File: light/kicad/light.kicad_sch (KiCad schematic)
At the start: 106 parts, among them U1 FT4232H, U11 TLV7103318DDSE, U14 74LVC1G07, U2 SN74AVC4T774RSVR, U3 SN74AVC4T774RSVR, U4 SN74AVC4T774RSVR, U5 74LVC1G07, U6 SN74AHC595QWBQBRQ1, U7 TLV75533PDBV, U8 TLV75533PDBV, U9 93LC56BT-I/OT, Y1 12MHz_7M-12.000MAAJ

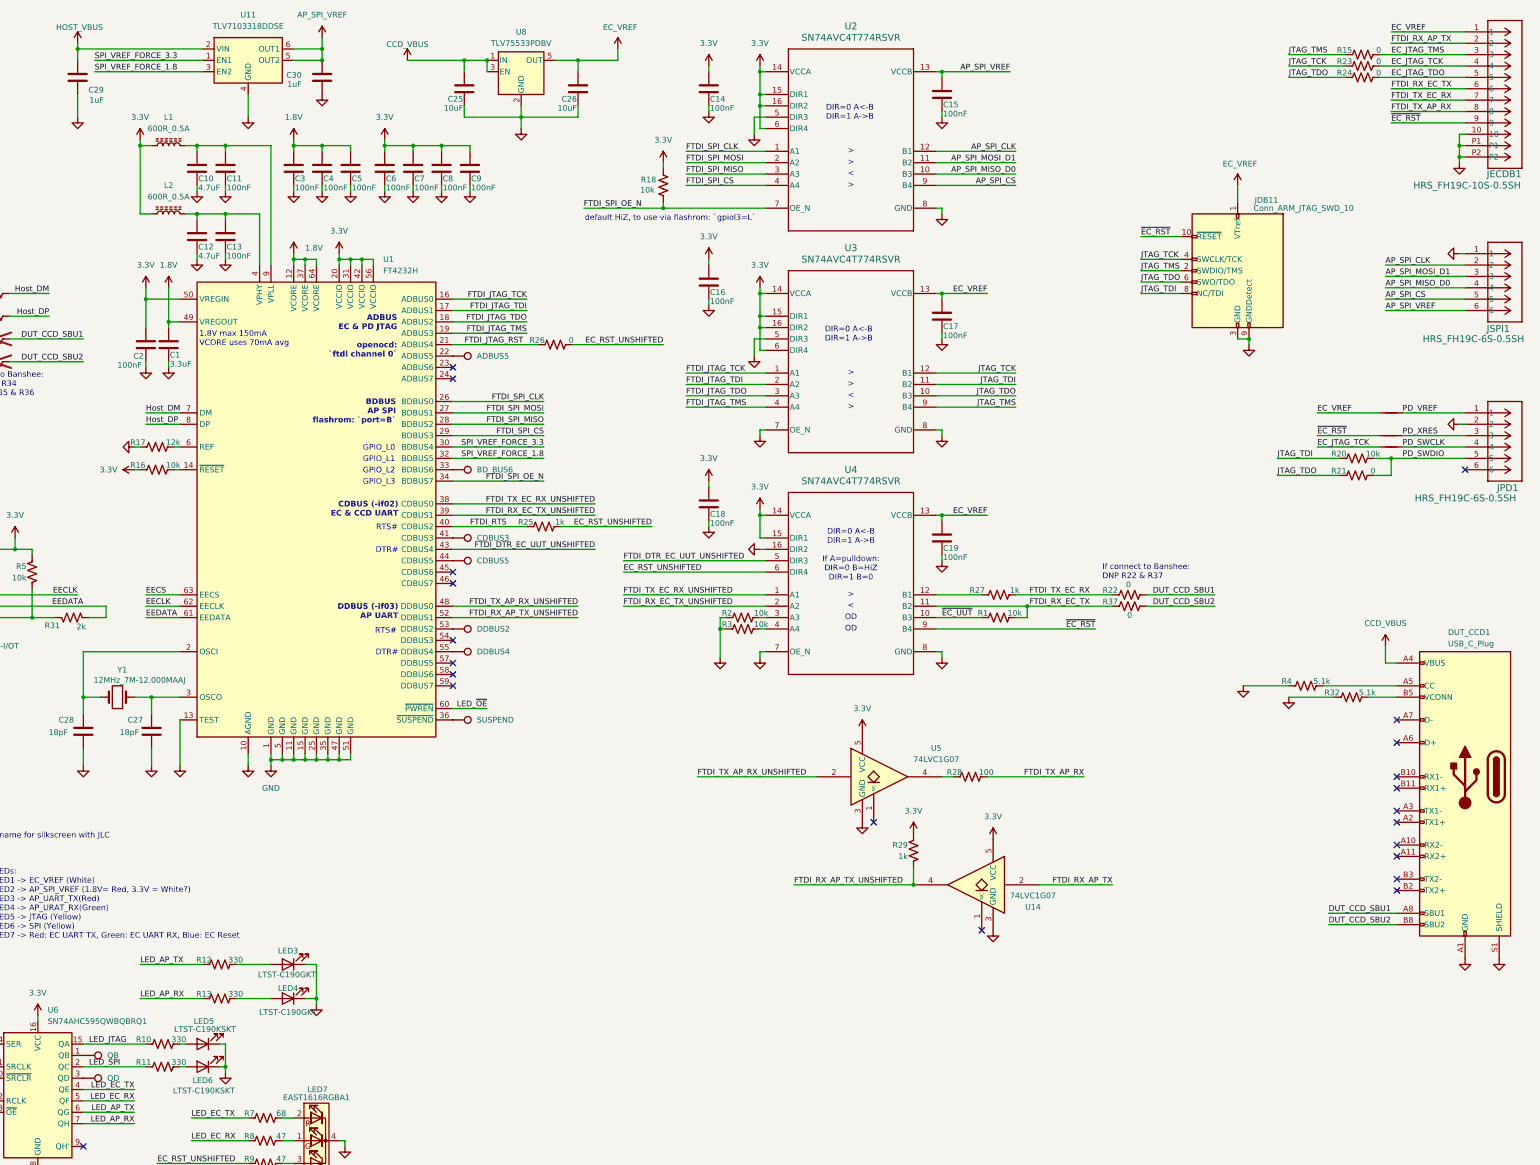
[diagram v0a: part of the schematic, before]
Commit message: kicad: renaming netname and fixing pin order of the connectors
11/05

1. Rename JTAG netname
2. Change pin order of JPD1, JSPI1, JECDB1
3. Remove TPs
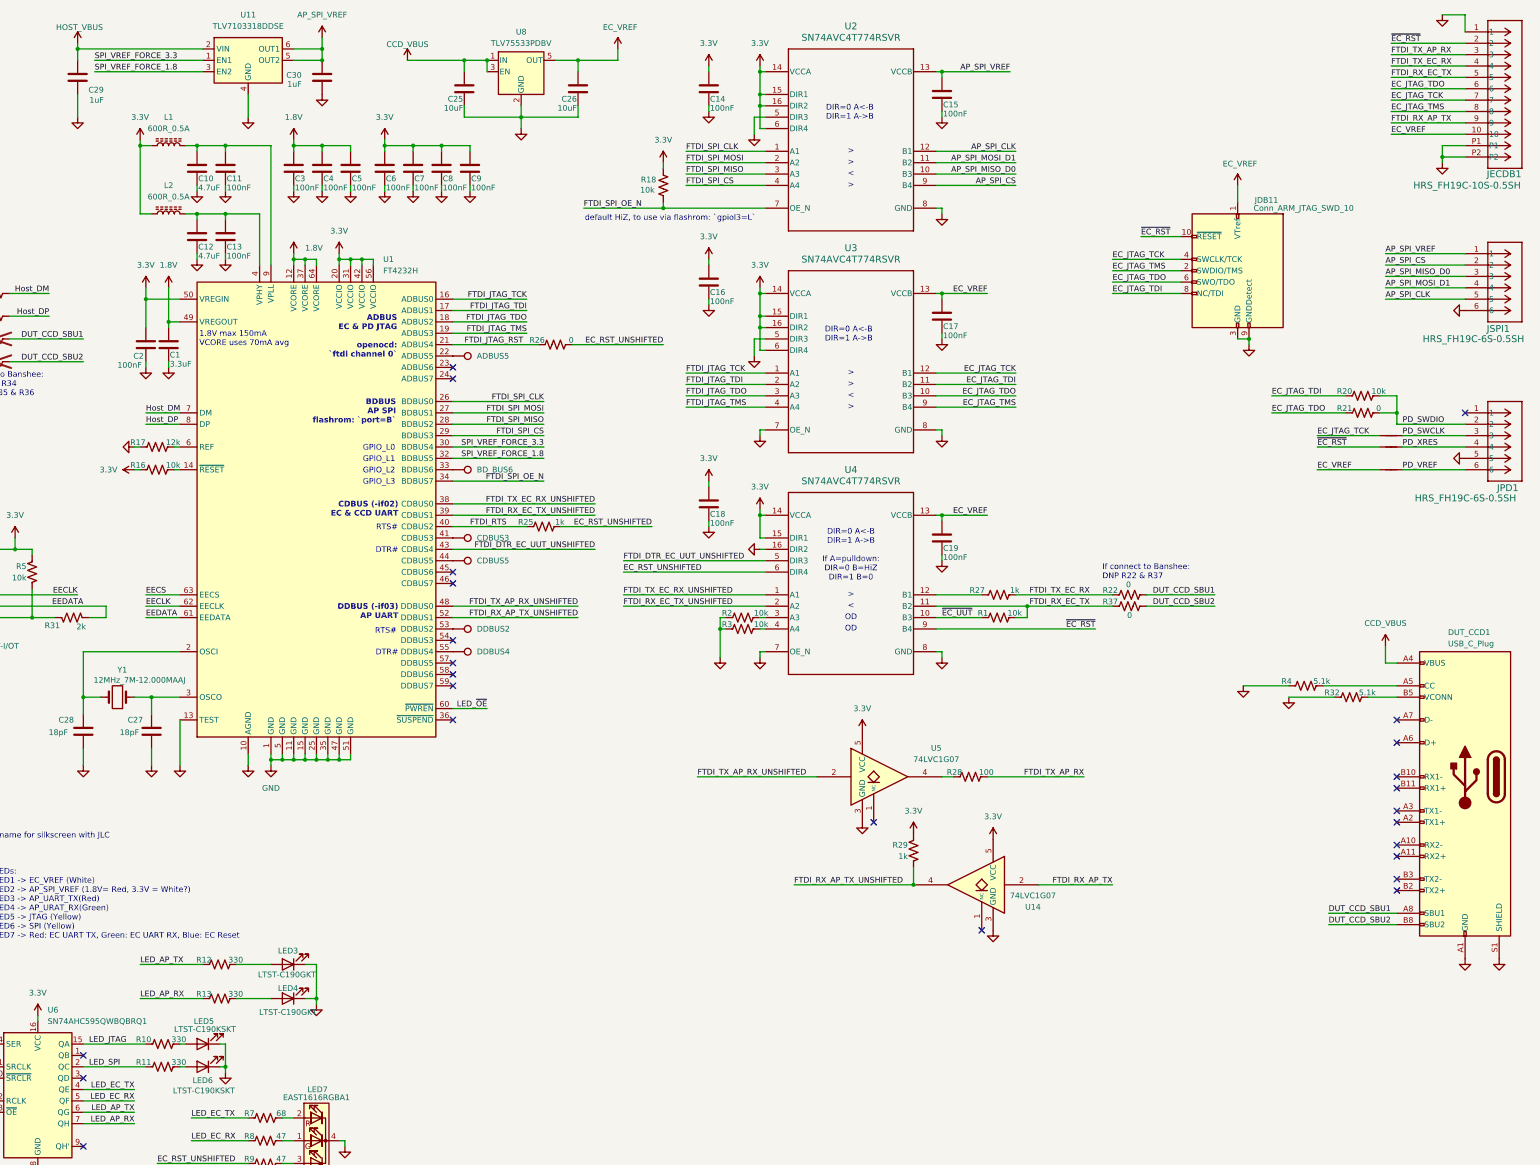
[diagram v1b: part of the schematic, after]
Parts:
- removed QB, QD, SUSPEND: TestPoint, TestPoint:TestPoint_Pad_D1.5mm, symbol Connector:TestPoint
- removed R15, R23, R24: 0, Resistor_SMD:R_0603_1608Metric, symbol Device:R_US
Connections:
- net JTAG_TCK is gone; now on net EC_JTAG_TCK: JDB11.4 (SWCLK/TCK), U3.12 (B1)
- net JTAG_TDO is gone; now on net EC_JTAG_TDO: JDB11.6 (SWO/TDO), R21.2, U3.10 (B3)
- net JTAG_TMS is gone; now on net EC_JTAG_TMS: JDB11.2 (SWDIO/TMS), U3.9 (B4)
- net AP_SPI_CLK: now also JSPI1.5; no longer JSPI1.2
- net AP_SPI_CS: now also JSPI1.2; no longer JSPI1.5
- net AP_SPI_MISO_D0: now also JSPI1.3; no longer JSPI1.4
- net AP_SPI_MOSI_D1: now also JSPI1.4; no longer JSPI1.3
- net AP_SPI_VREF: now also JSPI1.1; no longer JSPI1.6
- net EC_JTAG_TCK: now also JECDB1.7; no longer JECDB1.4
- net EC_JTAG_TDO: now also JECDB1.6; no longer JECDB1.5
- net EC_JTAG_TMS: now also JECDB1.8; no longer JECDB1.3
- net EC_VREF: now also JECDB1.10; no longer JECDB1.1
- net FTDI_RX_AP_TX: now also JECDB1.9; no longer JECDB1.2
- net FTDI_RX_EC_TX: now also JECDB1.5; no longer JECDB1.6
- net FTDI_TX_AP_RX: now also JECDB1.3; no longer JECDB1.8
- net FTDI_TX_EC_RX: now also JECDB1.4; no longer JECDB1.7
- net GND: now also JECDB1.1, JPD1.5, JSPI1.6; no longer JECDB1.10, JPD1.2, JSPI1.1
- net PD_SWCLK: now also JPD1.3; no longer JPD1.4
- net PD_SWDIO: now also JPD1.2; no longer JPD1.5
- net PD_VREF: now also JPD1.6; no longer JPD1.1
- net PD_XRES: now also JPD1.4; no longer JPD1.3
- net ~{EC_RST}: now also JECDB1.2; no longer JECDB1.9
- net JTAG_TDI renamed EC_JTAG_TDI
- no-connect marks 33 -> 36
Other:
- moved on the sheet: R20, R21

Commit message: kicad: add notes and update PCB file
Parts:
- C1, C10, C11, C12, C13, C14, C15, C16, C17, C18, C19, C2, C22, C23, C24, C25, C26, C27, C28, C29, C3, C30, C4, C5, C6, C7, C8, C9: footprint Capacitor_SMD:C_0603_1608Metric -> Capacitor_SMD:C_0201_0603Metric
- R1, R2, R20, R25, R26, R27, R28, R3: footprint Resistor_SMD:R_0603_1608Metric -> Resistor_SMD:R_0402_1005Metric
- R16, R17, R18, R21, R29, R31, R32, R4, R5, R6: footprint Resistor_SMD:R_0603_1608Metric -> Resistor_SMD:R_0201_0603Metric
- R35, R36: footprint (none) -> Resistor_SMD:R_0603_1608Metric; now fitted
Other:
- note added: "If connect to Banshee: R22 & R37 DNP R33 & R34 DNP R35 & R36 Populated else if:(default) R22 & R37 Populated R33 & R34 Populated R35 & R36 DNP"
- note removed: "If connect to Banshee: DNP R22 & R37"
- note removed: "If connect to Banshee: DNP R33 & R34 Populate R35 & R36"
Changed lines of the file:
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@@
 		)
 	)
-	(text "If connect to Banshee:\nDNP R22 & R37"
+	(text "If connect to Banshee:\nR22 & R37 DNP \nR33 & R34 DNP \nR35 & R36 Populated\n\nelse if:(default)\nR22 & R37 Populated \nR33 & R34 Populated \nR35 & R36 DNP\n"
 		(exclude_from_sim no)
-		(at 312.674 138.43 0)
+		(at 311.404 130.302 0)
 		(effects
 			(font
@@
 		)
 	)
-	(text "If connect to Banshee:\nDNP R33 & R34\nPopulate R35 & R36"
+	(text "If connect to Banshee:\nR22 & R37 DNP \nR33 & R34 DNP \nR35 & R36 Populated\n\nelse if:(default)\nR22 & R37 Populated \nR33 & R34 Populated \nR35 & R36 DNP\n"
 		(exclude_from_sim no)
-		(at 56.642 96.52 0)
+		(at 54.864 103.632 0)
 		(effects
 			(font
@@
 			)
 		)
-		(property "Footprint" "Resistor_SMD:R_0603_1608Metric"
+		(property "Footprint" "Resistor_SMD:R_0402_1005Metric"
 			(at 232.156 149.606 90)
 			(effects
@@
 			)
 		)
-		(property "Footprint" "Capacitor_SMD:C_0603_1608Metric"
+		(property "Footprint" "Capacitor_SMD:C_0201_0603Metric"
 			(at 139.3952 52.07 0)
 			(effects
@@
 			)
 		)
-		(property "Footprint" "Capacitor_SMD:C_0603_1608Metric"
+		(property "Footprint" "Capacitor_SMD:C_0201_0603Metric"
 			(at 277.8252 85.09 0)
 			(effects
@@
 			)
 		)
-		(property "Footprint" "Resistor_SMD:R_0603_1608Metric"
+		(property "Footprint" "Resistor_SMD:R_0201_0603Metric"
 			(at 213.614 51.816 90)
 			(effects
@@
 			)
 		)
-		(property "Footprint" "Resistor_SMD:R_0603_1608Metric"
+		(property "Footprint" "Resistor_SMD:R_0201_0603Metric"
 			(at 82.296 147.574 90)
 			(effects
@@
 			)
 		)
-		(property "Footprint" "Capacitor_SMD:C_0603_1608Metric"
+		(property "Footprint" "Capacitor_SMD:C_0201_0603Metric"
 			(at 169.2148 34.29 0)
 			(effects
@@
 			)
 		)
-		(property "Footprint" "Resistor_SMD:R_0603_1608Metric"
+		(property "Footprint" "Resistor_SMD:R_0201_0603Metric"
 			(at 72.644 138.684 90)
 			(effects
@@
 			)
 		)
-		(property "Footprint" "Capacitor_SMD:C_0603_1608Metric"
+		(property "Footprint" "Capacitor_SMD:C_0201_0603Metric"
 			(at 153.3652 52.07 0)
 			(effects
@@
 			)
 		)
-		(property "Footprint" "Capacitor_SMD:C_0603_1608Metric"
+		(property "Footprint" "Capacitor_SMD:C_0201_0603Metric"
 			(at 277.8252 35.56 0)
 			(effects
@@
 			)
 		)
-		(property "Footprint" "Capacitor_SMD:C_0603_1608Metric"
+		(property "Footprint" "Capacitor_SMD:C_0201_0603Metric"
 			(at 225.7552 127 0)
 			(effects
@@
 			)
 		)
-		(property "Footprint" "Resistor_SMD:R_0603_1608Metric"
+		(property "Footprint" "Resistor_SMD:R_0201_0603Metric"
 			(at 101.346 111.506 90)
 			(effects
@@
 			)
 		)
-		(property "Footprint" "Capacitor_SMD:C_0603_1608Metric"
+		(property "Footprint" "Capacitor_SMD:C_0201_0603Metric"
 			(at 277.8252 134.62 0)
 			(effects
@@
 			)
 		)
-		(property "Footprint" "Resistor_SMD:R_0603_1608Metric"
+		(property "Footprint" "Resistor_SMD:R_0402_1005Metric"
 			(at 187.706 129.286 90)
 			(effects
@@
 			)
 		)
-		(property "Footprint" "Capacitor_SMD:C_0603_1608Metric"
+		(property "Footprint" "Capacitor_SMD:C_0201_0603Metric"
 			(at 172.4152 52.07 0)
 			(effects
@@
 			)
 		)
-		(property "Footprint" "Resistor_SMD:R_0603_1608Metric"
+		(property "Footprint" "Resistor_SMD:R_0201_0603Metric"
 			(at 52.324 254.254 90)
 			(effects
@@
 			)
 		)
-		(property "Footprint" "Capacitor_SMD:C_0603_1608Metric"
+		(property "Footprint" "Capacitor_SMD:C_0201_0603Metric"
 			(at 194.6148 34.29 0)
 			(effects
@@
 			)
 		)
-		(property "Footprint" "Resistor_SMD:R_0603_1608Metric"
+		(property "Footprint" "Resistor_SMD:R_0402_1005Metric"
 			(at 282.956 185.166 90)
 			(effects
@@
 			)
 		)
-		(property "Footprint" "Resistor_SMD:R_0603_1608Metric"
+		(property "Footprint" "Resistor_SMD:R_0201_0603Metric"
 			(at 368.046 167.386 90)
 			(effects
@@
 			)
 		)
-		(property "Footprint" "Capacitor_SMD:C_0603_1608Metric"
+		(property "Footprint" "Capacitor_SMD:C_0201_0603Metric"
 			(at 117.8052 52.07 0)
 			(effects
@@
 			)
 		)
-		(property "Footprint" "Capacitor_SMD:C_0603_1608Metric"
+		(property "Footprint" "Capacitor_SMD:C_0201_0603Metric"
 			(at 82.8548 31.75 0)
 			(effects
@@
 		(in_bom yes)
 		(on_board yes)
-		(dnp yes)
+		(dnp no)
 		(property "Reference" "R35"
 			(at 60.452 85.344 90)
@@
 			)
 		)
-		(property "Footprint" ""
+		(property "Footprint" "Resistor_SMD:R_0603_1608Metric"
 			(at 64.516 87.376 90)
 			(effects
@@
 			)
 		)
-		(property "Footprint" "Resistor_SMD:R_0603_1608Metric"
+		(property "Footprint" "Resistor_SMD:R_0201_0603Metric"
 			(at 101.346 116.586 90)
 			(effects
@@
 			)
 		)
-		(property "Footprint" "Capacitor_SMD:C_0603_1608Metric"
+		(property "Footprint" "Capacitor_SMD:C_0201_0603Metric"
 			(at 43.4848 257.81 0)
 			(effects
@@
 			)
 		)
-		(property "Footprint" "Capacitor_SMD:C_0603_1608Metric"
+		(property "Footprint" "Capacitor_SMD:C_0201_0603Metric"
 			(at 57.4548 34.29 0)
 			(effects
@@
 			)
 		)
-		(property "Footprint" "Capacitor_SMD:C_0603_1608Metric"
+		(property "Footprint" "Capacitor_SMD:C_0201_0603Metric"
 			(at 105.1052 91.44 0)
 			(effects
@@
 			)
 		)
-		(property "Footprint" "Capacitor_SMD:C_0603_1608Metric"
+		(property "Footprint" "Capacitor_SMD:C_0201_0603Metric"
 			(at 225.7552 34.29 0)
 			(effects
@@
 			)
 		)
-		(property "Footprint" "Resistor_SMD:R_0603_1608Metric"
+		(property "Footprint" "Resistor_SMD:R_0201_0603Metric"
 			(at 357.886 164.846 90)
 			(effects
@@
 			)
 		)
-		(property "Footprint" "Capacitor_SMD:C_0603_1608Metric"
+		(property "Footprint" "Capacitor_SMD:C_0201_0603Metric"
 			(at 111.4552 67.31 0)
 			(effects
@@
 			)
 		)
-		(property "Footprint" "Capacitor_SMD:C_0603_1608Metric"
+		(property "Footprint" "Capacitor_SMD:C_0201_0603Metric"
 			(at 99.3648 170.18 0)
 			(effects
@@
 			)
 		)
-		(property "Footprint" "Capacitor_SMD:C_0603_1608Metric"
+		(property "Footprint" "Capacitor_SMD:C_0201_0603Metric"
 			(at 111.4552 52.07 0)
 			(effects
@@
 			)
 		)
-		(property "Footprint" "Capacitor_SMD:C_0603_1608Metric"
+		(property "Footprint" "Capacitor_SMD:C_0201_0603Metric"
 			(at 137.4648 31.75 0)
 			(effects
@@
 			)
 		)
-		(property "Footprint" "Capacitor_SMD:C_0603_1608Metric"
+		(property "Footprint" "Capacitor_SMD:C_0201_0603Metric"
 			(at 133.0452 52.07 0)
 			(effects
@@
 			)
 		)
-		(property "Footprint" "Capacitor_SMD:C_0603_1608Metric"
+		(property "Footprint" "Capacitor_SMD:C_0201_0603Metric"
 			(at 225.7552 77.47 0)
 			(effects
@@
 			)
 		)
-		(property "Footprint" "Capacitor_SMD:C_0603_1608Metric"
+		(property "Footprint" "Capacitor_SMD:C_0201_0603Metric"
 			(at 145.7452 52.07 0)
 			(effects
@@
 		(in_bom yes)
 		(on_board yes)
-		(dnp yes)
+		(dnp no)
 		(property "Reference" "R36"
 			(at 60.452 90.424 90)
@@
 			)
 		)
-		(property "Footprint" ""
+		(property "Footprint" "Resistor_SMD:R_0603_1608Metric"
 			(at 64.516 92.456 90)
 			(effects
@@
 			)
 		)
-		(property "Footprint" "Resistor_SMD:R_0603_1608Metric"
+		(property "Footprint" "Resistor_SMD:R_0402_1005Metric"
 			(at 232.156 152.146 90)
 			(effects
@@
 			)
 		)
-		(property "Footprint" "Resistor_SMD:R_0603_1608Metric"
+		(property "Footprint" "Resistor_SMD:R_0402_1005Metric"
 			(at 289.306 144.526 90)
 			(effects
@@
 			)
 		)
-		(property "Footprint" "Capacitor_SMD:C_0603_1608Metric"
+		(property "Footprint" "Capacitor_SMD:C_0201_0603Metric"
 			(at 86.0552 177.8 0)
 			(effects
@@
 			)
 		)
-		(property "Footprint" "Resistor_SMD:R_0603_1608Metric"
+		(property "Footprint" "Resistor_SMD:R_0201_0603Metric"
 			(at 269.494 200.914 90)
 			(effects
@@
 			)
 		)
-		(property "Footprint" "Resistor_SMD:R_0603_1608Metric"
+		(property "Footprint" "Resistor_SMD:R_0402_1005Metric"
 			(at 289.306 149.606 90)
 			(effects
@@
 			)
 		)
-		(property "Footprint" "Capacitor_SMD:C_0603_1608Metric"
+		(property "Footprint" "Capacitor_SMD:C_0201_0603Metric"
 			(at 166.0652 52.07 0)
 			(effects
@@
 			)
 		)
-		(property "Footprint" "Capacitor_SMD:C_0603_1608Metric"
+		(property "Footprint" "Capacitor_SMD:C_0201_0603Metric"
 			(at 159.7152 52.07 0)
 			(effects
@@
 			)
 		)
-		(property "Footprint" "Resistor_SMD:R_0603_1608Metric"
+		(property "Footprint" "Resistor_SMD:R_0201_0603Metric"
 			(at 370.586 103.886 90)
 			(effects
@@
 			)
 		)
-		(property "Footprint" "Capacitor_SMD:C_0603_1608Metric"
+		(property "Footprint" "Capacitor_SMD:C_0201_0603Metric"
 			(at 32.0548 34.29 0)
 			(effects
@@
 			)
 		)
-		(property "Footprint" "Capacitor_SMD:C_0603_1608Metric"
+		(property "Footprint" "Capacitor_SMD:C_0201_0603Metric"
 			(at 100.0252 91.44 0)
 			(effects
@@
 			)
 		)
-		(property "Footprint" "Resistor_SMD:R_0603_1608Metric"
+		(property "Footprint" "Resistor_SMD:R_0402_1005Metric"
 			(at 190.246 88.646 90)
 			(effects
@@
 			)
 		)
-		(property "Footprint" "Resistor_SMD:R_0603_1608Metric"
+		(property "Footprint" "Resistor_SMD:R_0402_1005Metric"
 			(at 370.586 100.076 90)
 			(effects
@@
 			)
 		)
-		(property "Footprint" "Capacitor_SMD:C_0603_1608Metric"
+		(property "Footprint" "Capacitor_SMD:C_0201_0603Metric"
 			(at 117.8052 67.31 0)
 			(effects

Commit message: kidcad: feedback implementation and updating boardfile version
12/16

1. Add a jumper for forcing power on to target device (J1)
2. add pull down on enable pins of FTDI. e.g. U11 (R15, R23)
3. add SPI Socket footprint  (TBD)
4. Add CC2 5.1k of Host connector (R24)
5. add pin header for EC Reset (J2)
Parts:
- added J1: Conn_01x03_Pin, symbol Connector:Conn_01x03_Pin
- added J2: Conn_01x02_Pin, Connector_PinHeader_2.54mm:PinHeader_1x02_P2.54mm_Vertical_SMD_Pin1Left, symbol Connector:Conn_01x02_Pin
- added J3: SPI Socket, ACES_50950-0084N-002, symbol Connector:Conn_01x09_Socket
- added R15, R23: 100k, Resistor_SMD:R_0402_1005Metric, symbol Device:R_US
- added R24: 5.1k, Resistor_SMD:R_0603_1608Metric, symbol Device:R_US
- JDB11: footprint Library_Myself:Conn_ARM_JTAG_SWD_10 -> Connector_PinHeader_1.27mm:PinHeader_2x05_P1.27mm_Vertical_SMD
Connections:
- net AP_SPI_CLK: now also J3.6 (Pin_6)
- net AP_SPI_CS: now also J3.1 (Pin_1)
- net AP_SPI_MISO_D0: now also J3.5 (Pin_5)
- net AP_SPI_MOSI_D1: now also J3.2 (Pin_2)
- net AP_SPI_VREF: now also J3.8 (Pin_8)
- net CCD_VBUS: now also J1.1 (Pin_1); no longer C25.1, U8.1 (IN), U8.3 (EN)
- net GND: now also J2.1 (Pin_1), J3.4 (Pin_4), J3.9 (Pin_9), R15.1, R23.1, R24.1
- net HOST_VBUS: now also J1.3 (Pin_3)
- net SPI_VREF_FORCE_1.8: now also R23.2
- net SPI_VREF_FORCE_3.3: now also R15.2
- net ~{EC_RST}: now also J2.2 (Pin_2)
- net at HOST1.B5 (CC2): now also R24.2
- new net: C25.1, J1.2 (Pin_2), U8.1 (IN), U8.3 (EN)
- no-connect marks 36 -> 37
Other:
- moved on the sheet: C29, JDB11, R30
